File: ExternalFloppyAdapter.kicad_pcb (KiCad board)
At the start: 2 copper layers, 22 parts, among them J1 Screw_Terminal_01x04, U3 74LS38, U4 74LS74

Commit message: Layout reworked
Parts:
- moved J_DRIVE1 63.8 mm to (114.3, 61.0)
- moved R5 63.0 mm to (156.2, 78.1), turned to -90 degrees
- moved R3 55.3 mm to (150.5, 78.1), turned to -90 degrees
- moved R6 50.0 mm to (144.8, 90.8), turned to 90 degrees
- moved C3 48.1 mm to (134.6, 59.1)
- moved U_AMIGA1 47.9 mm to (86.0, 80.4), turned to -90 degrees
- moved J_SELECT2 47.4 mm to (146.1, 59.7), turned to 90 degrees
- moved R1 39.1 mm to (127.0, 53.3), turned to -90 degrees
- moved R2 36.6 mm to (121.9, 55.9), turned to -90 degrees
- moved R10 33.2 mm to (127.0, 103.5), turned to 90 degrees
- moved U4 31.8 mm to (132.1, 87.6)
- moved R4 31.4 mm to (127.0, 88.3), turned to 90 degrees
- moved J1 30.1 mm to (145.4, 101.0)
- moved J_SELECT3 28.1 mm to (146.1, 72.4), turned to 90 degrees
- moved R9 27.0 mm to (121.9, 103.5), turned to 90 degrees
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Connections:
- net Net-(J_DRIVE1-Pin_3) renamed /~{SEL2}
- J_DRIVE1 pad 1: Net-(J_DRIVE1-Pin_1) -> /~{SEL3}
- J_DRIVE1 pad 5: Net-(J_DRIVE1-Pin_5) -> /~{SEL1}
- U_AMIGA1 pad 20: Net-(J_DRIVE1-Pin_5) -> /~{SEL3}
- U_AMIGA1 pad 21: Net-(J_DRIVE1-Pin_1) -> /~{SEL1}
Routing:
- net GND: track 0.00 -> 186.9 mm, vias 0 -> 1
- net +5V: track 0.00 -> 177.9 mm
- net ~{WPRO}: track 0.00 -> 124.9 mm, vias 0 -> 1
- net /~{INDEX}: track 0.00 -> 117.7 mm, vias 0 -> 2
- net /~{DIR}: track 0.00 -> 116.8 mm, vias 0 -> 1
- net ~{DKRD}: track 0.00 -> 116.2 mm, vias 0 -> 1
- net /~{STEP}: track 0.00 -> 114.6 mm, vias 0 -> 1
- net /~{DKWD}: track 0.00 -> 113.7 mm, vias 0 -> 1
- net /~{DKWE}: track 0.00 -> 113.6 mm, vias 0 -> 1
- net ~{TKO}: track 0.00 -> 112.7 mm, vias 0 -> 2
- net /~{SIDE}: track 0.00 -> 112.3 mm, vias 0 -> 1
- net Net-(J_SELECT1-Pin_2): track 0.00 -> 81.7 mm, vias 0 -> 1
- net ~{CHNG}: track 0.00 -> 81.0 mm, vias 0 -> 1
- net Net-(J_SELECT1-Pin_1): track 0.00 -> 63.9 mm, vias 0 -> 1
- net Net-(J_DRIVE1-Pin_2): track 0.00 -> 54.4 mm, vias 0 -> 1
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- added copper zone on B.Cu, net GND
- added copper zone on F.Cu, net GND
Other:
- board outline added: 81.3 x 65.4 mm

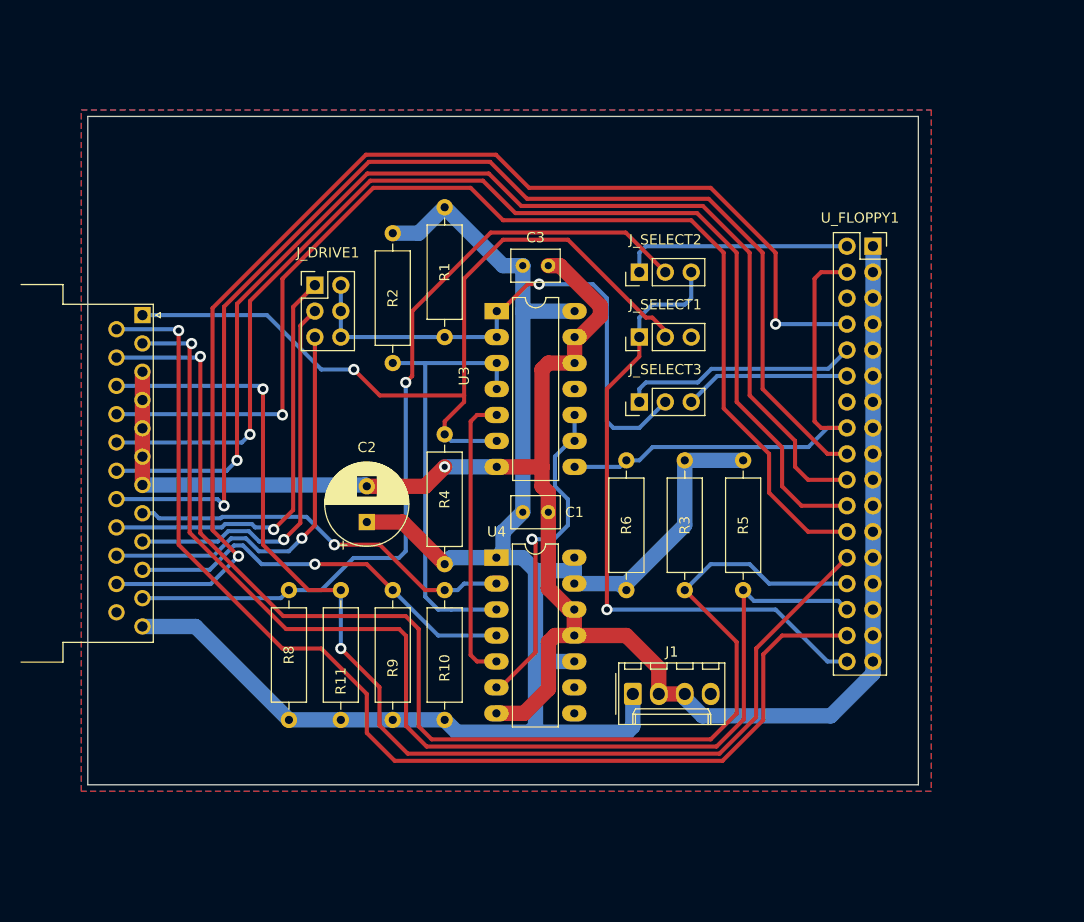
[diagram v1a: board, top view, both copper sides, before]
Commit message: Floppy connector changed, layout improved
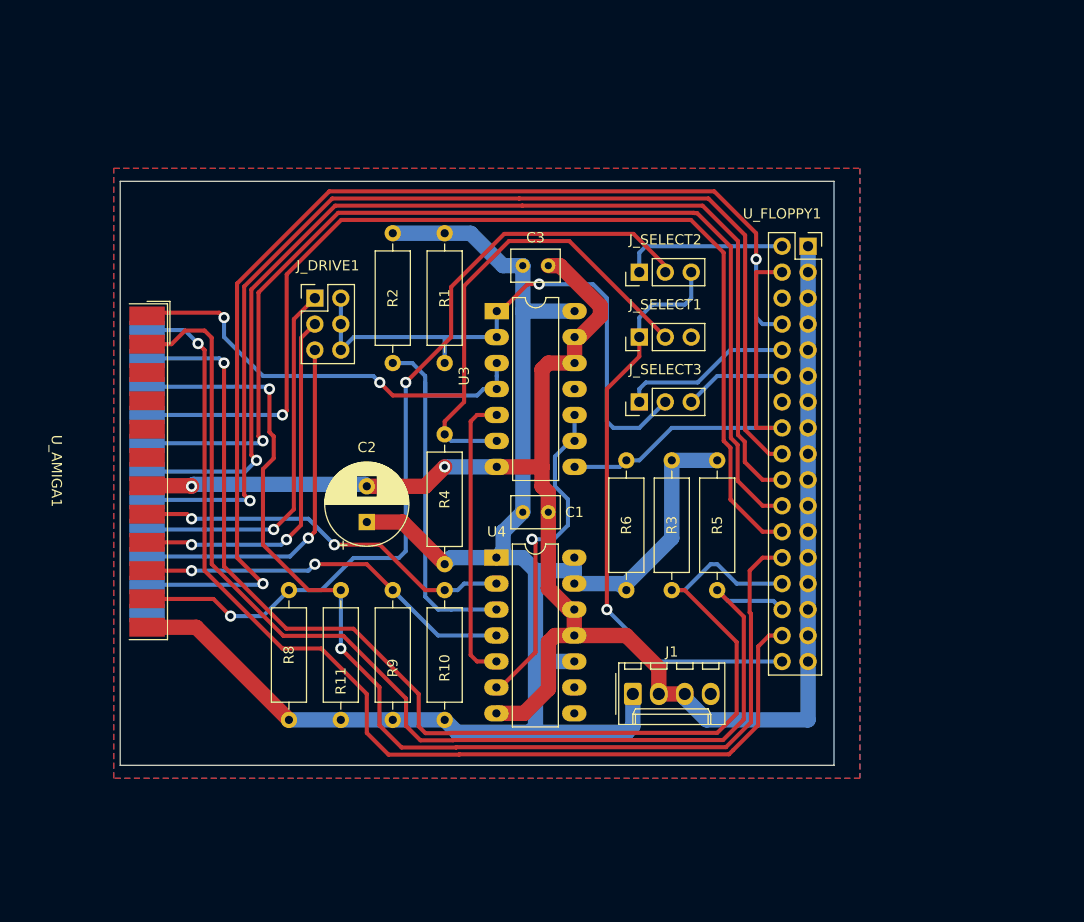
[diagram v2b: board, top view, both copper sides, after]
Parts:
- U_AMIGA1: footprint Amiga500:ExternalFloppyConnector -> Amiga500:ExternalFloppyConnectorEdgeMount
- moved U_AMIGA1 8.04 mm to (94.0, 79.1)
- moved U_FLOPPY1 6.35 mm to (162.6, 57.1)
- moved R5 2.54 mm to (153.7, 78.1)
- moved R1 2.54 mm to (127.0, 55.9)
- moved R3 1.27 mm to (149.2, 78.1)
- moved J_DRIVE1 1.27 mm to (114.3, 62.2)
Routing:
- net GND: track 186.9 -> 172.2 mm, vias 1 -> 2
- net ~{WPRO}: track 124.9 -> 115.3 mm
- net /~{DKWE}: track 113.6 -> 104.4 mm
- net /~{SIDE}: track 112.3 -> 103.6 mm
- net /~{INDEX}: track 117.7 -> 109.1 mm
- net /~{DKWD}: track 113.7 -> 105.5 mm
- net /~{STEP}: track 114.6 -> 106.8 mm
- net /~{DIR}: track 116.8 -> 109.0 mm
- net Net-(U_FLOPPY1-~{MOTEB}): track 49.1 -> 42.2 mm
- net Net-(J_SELECT3-Pin_1): track 23.2 -> 16.8 mm
- net Net-(J_SELECT3-Pin_3): track 16.3 -> 9.94 mm
- net Net-(J_SELECT2-Pin_1): track 22.5 -> 16.1 mm
- net Net-(J_SELECT1-Pin_1): track 63.9 -> 57.5 mm
- net /~{SEL1}: track 40.1 -> 35.2 mm
- net +5V: track 177.9 -> 173.5 mm
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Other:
- board size 81.3 x 65.4 mm -> 69.8 x 57.2 mm
